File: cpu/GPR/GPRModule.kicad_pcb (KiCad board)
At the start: 2 copper layers, 139.7 x 64.3 mm, 67 parts, among them J1 Interconnect 1, J2 Interconnect 2, U1 74HCT574, U10 74LS245, U11 74LS245, U12 74LS245, U13 74LS126, U2 74HCT574, U3 74LS14, U5 74LS245, U6 74LS245, U7 74LS245, U8 74LS245, U9 74LS245

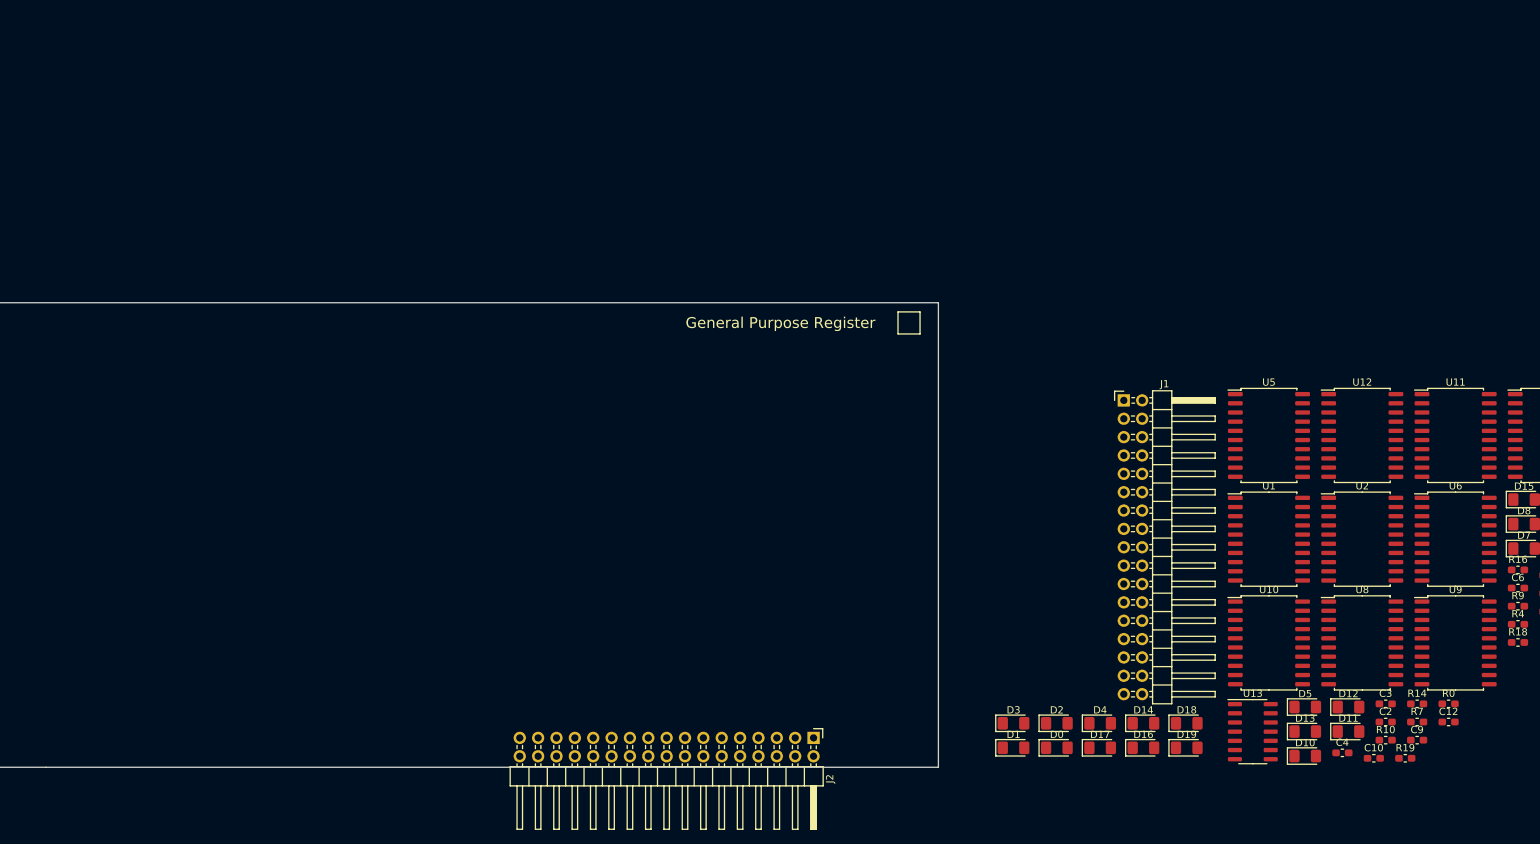
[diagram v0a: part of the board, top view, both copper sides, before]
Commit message: ALU and constant register first version
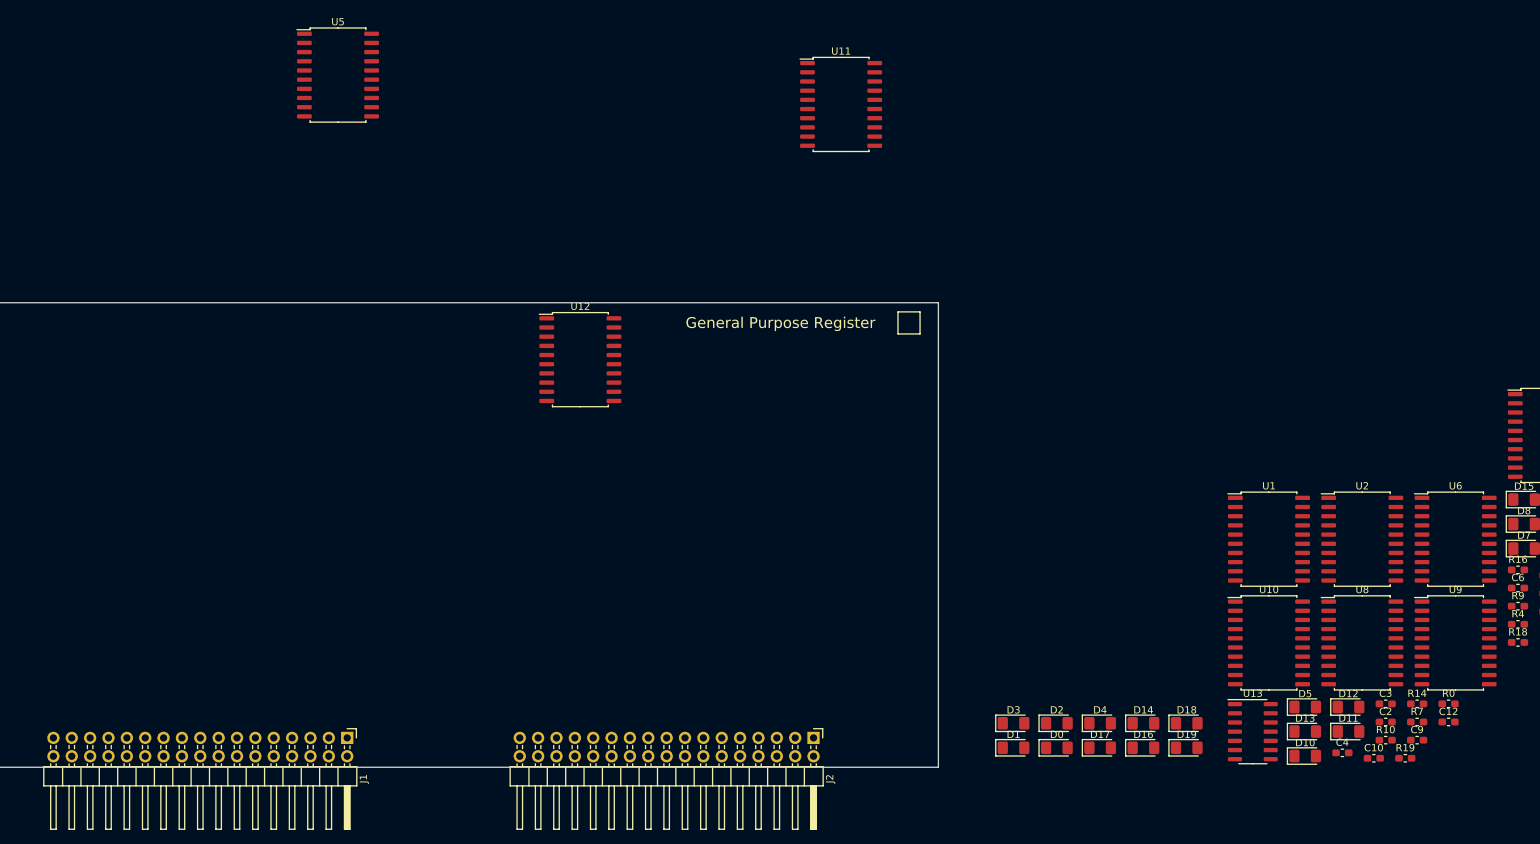
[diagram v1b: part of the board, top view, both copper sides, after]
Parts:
- moved U5 138.1 mm to (148.1, 32.3)
- moved J1 117.1 mm to (149.4, 124.0), turned to 270 degrees
- moved U12 108.7 mm to (181.6, 71.6)
- moved U11 96.6 mm to (217.7, 36.3)
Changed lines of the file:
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@@
   )
   (module Connector_PinHeader_2.54mm:PinHeader_2x17_P2.54mm_Horizontal (layer F.Cu)
-    (at 256.789001 77.263001)
+    (at 149.352 123.952 270)
     (descr "Through hole angled pin header, 2x17, 2.54mm pitch, 6mm pin length, double rows")
     (tags "Through hole angled pin header THT 2x17 2.54mm double row")
-    (fp_text reference J1 (at 5.655 -2.27) (layer F.SilkS)
-      (effects (font (size 1 1) (thickness 0.15)))
-    )
-    (fp_text value "Interconnect 1" (at 5.655 42.91) (layer F.Fab)
-      (effects (font (size 1 1) (thickness 0.15)))
-    )
-    (fp_text user %R (at 5.31 20.32 90) (layer F.Fab)
+    (fp_text reference J1 (at 5.655 -2.27 90) (layer F.SilkS)
+      (effects (font (size 1 1) (thickness 0.15)))
+    )
+    (fp_text value "Interconnect 1" (at 5.655 42.91 90) (layer F.Fab)
+      (effects (font (size 1 1) (thickness 0.15)))
+    )
+    (fp_text user %R (at 5.31 20.32) (layer F.Fab)
       (effects (font (size 1 1) (thickness 0.15)))
     )
@@
     (fp_line (start 6.58 -1.27) (end 6.58 41.91) (layer F.Fab) (width 0.1))
     (fp_line (start 4.675 -1.27) (end 6.58 -1.27) (layer F.Fab) (width 0.1))
-    (pad 34 thru_hole oval (at 2.54 40.64) (size 1.7 1.7) (drill 1) (layers *.Cu *.Mask)
+    (pad 34 thru_hole oval (at 2.54 40.64 270) (size 1.7 1.7) (drill 1) (layers *.Cu *.Mask)
       (net 2 +5V))
-    (pad 33 thru_hole oval (at 0 40.64) (size 1.7 1.7) (drill 1) (layers *.Cu *.Mask)
-      (net 1 GND))
-    (pad 32 thru_hole oval (at 2.54 38.1) (size 1.7 1.7) (drill 1) (layers *.Cu *.Mask)
+    (pad 33 thru_hole oval (at 0 40.64 270) (size 1.7 1.7) (drill 1) (layers *.Cu *.Mask)
+      (net 1 GND))
+    (pad 32 thru_hole oval (at 2.54 38.1 270) (size 1.7 1.7) (drill 1) (layers *.Cu *.Mask)
       (net 94 /d_bus_00))
-    (pad 31 thru_hole oval (at 0 38.1) (size 1.7 1.7) (drill 1) (layers *.Cu *.Mask)
+    (pad 31 thru_hole oval (at 0 38.1 270) (size 1.7 1.7) (drill 1) (layers *.Cu *.Mask)
       (net 19 /CLK))
-    (pad 30 thru_hole oval (at 2.54 35.56) (size 1.7 1.7) (drill 1) (layers *.Cu *.Mask)
+    (pad 30 thru_hole oval (at 2.54 35.56 270) (size 1.7 1.7) (drill 1) (layers *.Cu *.Mask)
       (net 95 /d_bus_01))
-    (pad 29 thru_hole oval (at 0 35.56) (size 1.7 1.7) (drill 1) (layers *.Cu *.Mask)
+    (pad 29 thru_hole oval (at 0 35.56 270) (size 1.7 1.7) (drill 1) (layers *.Cu *.Mask)
       (net 20 /~CLK))
-    (pad 28 thru_hole oval (at 2.54 33.02) (size 1.7 1.7) (drill 1) (layers *.Cu *.Mask)
+    (pad 28 thru_hole oval (at 2.54 33.02 270) (size 1.7 1.7) (drill 1) (layers *.Cu *.Mask)
       (net 96 /d_bus_02))
-    (pad 27 thru_hole oval (at 0 33.02) (size 1.7 1.7) (drill 1) (layers *.Cu *.Mask)
+    (pad 27 thru_hole oval (at 0 33.02 270) (size 1.7 1.7) (drill 1) (layers *.Cu *.Mask)
       (net 21 /HLT))
-    (pad 26 thru_hole oval (at 2.54 30.48) (size 1.7 1.7) (drill 1) (layers *.Cu *.Mask)
+    (pad 26 thru_hole oval (at 2.54 30.48 270) (size 1.7 1.7) (drill 1) (layers *.Cu *.Mask)
       (net 97 /d_bus_03))
-    (pad 25 thru_hole oval (at 0 30.48) (size 1.7 1.7) (drill 1) (layers *.Cu *.Mask)
+    (pad 25 thru_hole oval (at 0 30.48 270) (size 1.7 1.7) (drill 1) (layers *.Cu *.Mask)
       (net 114 /~DBG))
-    (pad 24 thru_hole oval (at 2.54 27.94) (size 1.7 1.7) (drill 1) (layers *.Cu *.Mask)
+    (pad 24 thru_hole oval (at 2.54 27.94 270) (size 1.7 1.7) (drill 1) (layers *.Cu *.Mask)
       (net 98 /d_bus_04))
-    (pad 23 thru_hole oval (at 0 27.94) (size 1.7 1.7) (drill 1) (layers *.Cu *.Mask)
+    (pad 23 thru_hole oval (at 0 27.94 270) (size 1.7 1.7) (drill 1) (layers *.Cu *.Mask)
       (net 22 /RST))
-    (pad 22 thru_hole oval (at 2.54 25.4) (size 1.7 1.7) (drill 1) (layers *.Cu *.Mask)
+    (pad 22 thru_hole oval (at 2.54 25.4 270) (size 1.7 1.7) (drill 1) (layers *.Cu *.Mask)
       (net 99 /d_bus_05))
-    (pad 21 thru_hole oval (at 0 25.4) (size 1.7 1.7) (drill 1) (layers *.Cu *.Mask)
+    (pad 21 thru_hole oval (at 0 25.4 270) (size 1.7 1.7) (drill 1) (layers *.Cu *.Mask)
       (net 115 "Net-(J1-Pad21)"))
-    (pad 20 thru_hole oval (at 2.54 22.86) (size 1.7 1.7) (drill 1) (layers *.Cu *.Mask)
+    (pad 20 thru_hole oval (at 2.54 22.86 270) (size 1.7 1.7) (drill 1) (layers *.Cu *.Mask)
       (net 100 /d_bus_06))
-    (pad 19 thru_hole oval (at 0 22.86) (size 1.7 1.7) (drill 1) (layers *.Cu *.Mask)
+    (pad 19 thru_hole oval (at 0 22.86 270) (size 1.7 1.7) (drill 1) (layers *.Cu *.Mask)
       (net 116 "Net-(J1-Pad19)"))
-    (pad 18 thru_hole oval (at 2.54 20.32) (size 1.7 1.7) (drill 1) (layers *.Cu *.Mask)
+    (pad 18 thru_hole oval (at 2.54 20.32 270) (size 1.7 1.7) (drill 1) (layers *.Cu *.Mask)
       (net 101 /d_bus_07))
-    (pad 17 thru_hole oval (at 0 20.32) (size 1.7 1.7) (drill 1) (layers *.Cu *.Mask)
+    (pad 17 thru_hole oval (at 0 20.32 270) (size 1.7 1.7) (drill 1) (layers *.Cu *.Mask)
       (net 117 "Net-(J1-Pad17)"))
-    (pad 16 thru_hole oval (at 2.54 17.78) (size 1.7 1.7) (drill 1) (layers *.Cu *.Mask)
+    (pad 16 thru_hole oval (at 2.54 17.78 270) (size 1.7 1.7) (drill 1) (layers *.Cu *.Mask)
       (net 102 /d_bus_08))
-    (pad 15 thru_hole oval (at 0 17.78) (size 1.7 1.7) (drill 1) (layers *.Cu *.Mask)
+    (pad 15 thru_hole oval (at 0 17.78 270) (size 1.7 1.7) (drill 1) (layers *.Cu *.Mask)
       (net 118 "Net-(J1-Pad15)"))
-    (pad 14 thru_hole oval (at 2.54 15.24) (size 1.7 1.7) (drill 1) (layers *.Cu *.Mask)
+    (pad 14 thru_hole oval (at 2.54 15.24 270) (size 1.7 1.7) (drill 1) (layers *.Cu *.Mask)
       (net 103 /d_bus_09))
-    (pad 13 thru_hole oval (at 0 15.24) (size 1.7 1.7) (drill 1) (layers *.Cu *.Mask)
+    (pad 13 thru_hole oval (at 0 15.24 270) (size 1.7 1.7) (drill 1) (layers *.Cu *.Mask)
       (net 119 "Net-(J1-Pad13)"))
-    (pad 12 thru_hole oval (at 2.54 12.7) (size 1.7 1.7) (drill 1) (layers *.Cu *.Mask)
+    (pad 12 thru_hole oval (at 2.54 12.7 270) (size 1.7 1.7) (drill 1) (layers *.Cu *.Mask)
       (net 104 /d_bus_10))
-    (pad 11 thru_hole oval (at 0 12.7) (size 1.7 1.7) (drill 1) (layers *.Cu *.Mask)
+    (pad 11 thru_hole oval (at 0 12.7 270) (size 1.7 1.7) (drill 1) (layers *.Cu *.Mask)
       (net 120 "Net-(J1-Pad11)"))
-    (pad 10 thru_hole oval (at 2.54 10.16) (size 1.7 1.7) (drill 1) (layers *.Cu *.Mask)
+    (pad 10 thru_hole oval (at 2.54 10.16 270) (size 1.7 1.7) (drill 1) (layers *.Cu *.Mask)
       (net 105 /d_bus_11))
-    (pad 9 thru_hole oval (at 0 10.16) (size 1.7 1.7) (drill 1) (layers *.Cu *.Mask)
+    (pad 9 thru_hole oval (at 0 10.16 270) (size 1.7 1.7) (drill 1) (layers *.Cu *.Mask)
       (net 121 "Net-(J1-Pad9)"))
-    (pad 8 thru_hole oval (at 2.54 7.62) (size 1.7 1.7) (drill 1) (layers *.Cu *.Mask)
+    (pad 8 thru_hole oval (at 2.54 7.62 270) (size 1.7 1.7) (drill 1) (layers *.Cu *.Mask)
       (net 106 /d_bus_12))
-    (pad 7 thru_hole oval (at 0 7.62) (size 1.7 1.7) (drill 1) (layers *.Cu *.Mask)
+    (pad 7 thru_hole oval (at 0 7.62 270) (size 1.7 1.7) (drill 1) (layers *.Cu *.Mask)
       (net 107 /y_bus_write))
-    (pad 6 thru_hole oval (at 2.54 5.08) (size 1.7 1.7) (drill 1) (layers *.Cu *.Mask)
+    (pad 6 thru_hole oval (at 2.54 5.08 270) (size 1.7 1.7) (drill 1) (layers *.Cu *.Mask)
       (net 108 /d_bus_13))
-    (pad 5 thru_hole oval (at 0 5.08) (size 1.7 1.7) (drill 1) (layers *.Cu *.Mask)
+    (pad 5 thru_hole oval (at 0 5.08 270) (size 1.7 1.7) (drill 1) (layers *.Cu *.Mask)
       (net 109 /x_bus_write))
-    (pad 4 thru_hole oval (at 2.54 2.54) (size 1.7 1.7) (drill 1) (layers *.Cu *.Mask)
+    (pad 4 thru_hole oval (at 2.54 2.54 270) (size 1.7 1.7) (drill 1) (layers *.Cu *.Mask)
       (net 110 /d_bus_14))
-    (pad 3 thru_hole oval (at 0 2.54) (size 1.7 1.7) (drill 1) (layers *.Cu *.Mask)
+    (pad 3 thru_hole oval (at 0 2.54 270) (size 1.7 1.7) (drill 1) (layers *.Cu *.Mask)
       (net 111 /d_bus_write))
-    (pad 2 thru_hole oval (at 2.54 0) (size 1.7 1.7) (drill 1) (layers *.Cu *.Mask)
+    (pad 2 thru_hole oval (at 2.54 0 270) (size 1.7 1.7) (drill 1) (layers *.Cu *.Mask)
       (net 112 /d_bus_15))
-    (pad 1 thru_hole rect (at 0 0) (size 1.7 1.7) (drill 1) (layers *.Cu *.Mask)
+    (pad 1 thru_hole rect (at 0 0 270) (size 1.7 1.7) (drill 1) (layers *.Cu *.Mask)
       (net 113 /d_bus_read))
     (model ${KISYS3DMOD}/Connector_PinHeader_2.54mm.3dshapes/PinHeader_2x17_P2.54mm_Horizontal.wrl
@@
   )
   (module Package_SO:SOIC-20W_7.5x12.8mm_P1.27mm (layer F.Cu)
-    (at 276.869001 82.113001)
+    (at 148.082 32.258)
     (descr "SOIC, 20 Pin (JEDEC MS-013AC, https://www.analog.com/media/en/package-pcb-resources/package/233848rw_20.pdf), generated with kicad-footprint-generator ipc_gullwing_generator.py")
     (tags "SOIC SO")
@@
   )
   (module Package_SO:SOIC-20W_7.5x12.8mm_P1.27mm (layer F.Cu)
-    (at 302.689001 82.113001)
+    (at 217.678 36.322)
     (descr "SOIC, 20 Pin (JEDEC MS-013AC, https://www.analog.com/media/en/package-pcb-resources/package/233848rw_20.pdf), generated with kicad-footprint-generator ipc_gullwing_generator.py")
     (tags "SOIC SO")
@@
   )
   (module Package_SO:SOIC-20W_7.5x12.8mm_P1.27mm (layer F.Cu)
-    (at 289.779001 82.113001)
+    (at 181.61 71.628)
     (descr "SOIC, 20 Pin (JEDEC MS-013AC, https://www.analog.com/media/en/package-pcb-resources/package/233848rw_20.pdf), generated with kicad-footprint-generator ipc_gullwing_generator.py")
     (tags "SOIC SO")

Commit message: Completed GPR 1.2 PCB and started lots of other things. * Started ALU * Updated Constant Reg * Completed v1.2 GPR * Added random symbols * Updated Memory * Updated plots
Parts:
- removed C12, C13: 0.1uF, Capacitor_SMD:C_0603_1608Metric_Pad1.05x0.95mm_HandSolder
- removed J2: Interconnect 2, Connector_PinHeader_2.54mm:PinHeader_2x17_P2.54mm_Horizontal
- removed R0, R1, R10, R11, R12, R13, R14, R15, R2, R3, R4, R5, R6, R7, R8, R9: 220R, Resistor_SMD:R_0603_1608Metric_Pad1.05x0.95mm_HandSolder
- removed U12: 74LS245, Package_SO:SOIC-20W_7.5x12.8mm_P1.27mm
- removed U13: 74LS126, Package_SO:SOIC-14_3.9x8.7mm_P1.27mm
- added REF**: OSHW, Symbol:OSHW-Logo2_7.3x6mm_SilkScreen, F.Cu at (178.2, 69.5)
- added RN1: 220R, Resistor_SMD:R_Array_Convex_8x0602, F.Cu at (100.2, 70.0)
- added RN2: 220R, Resistor_SMD:R_Array_Convex_8x0602, F.Cu at (128.8, 70.0)
- added U4: 74LS245, Package_SO:SOIC-20W_7.5x12.8mm_P1.27mm, F.Cu at (156.2, 92.6)
- J1: value Interconnect 1 -> Interconnect; footprint Connector_PinHeader_2.54mm:PinHeader_2x17_P2.54mm_Horizontal -> Connector_PCBEdge:BUS_PCI
- U11: value 74LS245 -> 74LS126; footprint Package_SO:SOIC-20W_7.5x12.8mm_P1.27mm -> Package_SO:SOIC-14_3.9x8.7mm_P1.27mm
- U3: value 74LS14 -> 74LS245; footprint Package_SO:SOIC-14_3.9x8.7mm_P1.27mm -> Package_SO:SOIC-20W_7.5x12.8mm_P1.27mm
- moved C8 221.7 mm to (102.6, 84.8)
- moved D15 220.3 mm to (93.9, 60.9), turned to 270 degrees
- moved U7 218.5 mm to (98.8, 109.6)
- moved C7 214.9 mm to (102.6, 101.8)
- moved D9 204.1 mm to (116.2, 60.9), turned to 270 degrees
- moved D6 197.0 mm to (129.8, 60.9), turned to 270 degrees
- moved U9 195.4 mm to (110.8, 74.2)
- moved D8 195.1 mm to (120.0, 60.9), turned to 270 degrees
- moved D12 192.1 mm to (105.0, 60.9), turned to 270 degrees
- moved U8 191.8 mm to (98.8, 92.6)
- moved D13 191.0 mm to (101.3, 60.9), turned to 270 degrees
- moved D7 189.8 mm to (126.0, 60.9), turned to 270 degrees
- moved D11 189.6 mm to (108.8, 60.9), turned to 270 degrees
- moved C9 186.8 mm to (119.1, 68.5), turned to 180 degrees
- moved C5 186.3 mm to (131.1, 101.8)
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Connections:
- C1 pad 1: +5V -> GND
- C1 pad 2: GND -> +5V
- C10 pad 1: +5V -> GND
- C10 pad 2: GND -> +5V
- C11 pad 1: +5V -> GND
- C11 pad 2: GND -> +5V
- C2 pad 1: +5V -> GND
- C2 pad 2: GND -> +5V
- C3 pad 1: +5V -> GND
- C3 pad 2: GND -> +5V
- C4 pad 1: +5V -> GND
- C4 pad 2: GND -> +5V
- C5 pad 1: +5V -> GND
- C5 pad 2: GND -> +5V
- C6 pad 1: +5V -> GND
- C6 pad 2: GND -> +5V
- C7 pad 1: +5V -> GND
- C7 pad 2: GND -> +5V
- C8 pad 1: +5V -> GND
- C8 pad 2: GND -> +5V
- C9 pad 1: +5V -> GND
- C9 pad 2: GND -> +5V
- D0 pad 1: Net-(D0-Pad1) -> GND
- D0 pad 2: /display_00 -> Net-(D0-Pad2)
- D1 pad 1: Net-(D1-Pad1) -> GND
- D1 pad 2: /display_01 -> Net-(D1-Pad2)
- D10 pad 1: Net-(D10-Pad1) -> GND
- D10 pad 2: /display_10 -> Net-(D10-Pad2)
- D11 pad 1: Net-(D11-Pad1) -> GND
- D11 pad 2: /display_11 -> Net-(D11-Pad2)
- D12 pad 1: Net-(D12-Pad1) -> GND
- D12 pad 2: /display_12 -> Net-(D12-Pad2)
- D13 pad 1: Net-(D13-Pad1) -> GND
- D13 pad 2: /display_13 -> Net-(D13-Pad2)
- D14 pad 1: Net-(D14-Pad1) -> GND
- D14 pad 2: /display_14 -> Net-(D14-Pad2)
- D15 pad 1: Net-(D15-Pad1) -> GND
- D15 pad 2: /display_15 -> Net-(D15-Pad2)
- D16 pad 2: Net-(D16-Pad2) -> +5V
- D17 pad 2: Net-(D17-Pad2) -> +5V
- D18 pad 2: Net-(D18-Pad2) -> +5V
- D19 pad 1: Net-(D19-Pad1) -> GND
- D2 pad 1: Net-(D2-Pad1) -> GND
- D2 pad 2: /display_02 -> Net-(D2-Pad2)
- D3 pad 1: Net-(D3-Pad1) -> GND
- D3 pad 2: /display_03 -> Net-(D3-Pad2)
- D4 pad 1: Net-(D4-Pad1) -> GND
- D4 pad 2: /display_04 -> Net-(D4-Pad2)
- D5 pad 1: Net-(D5-Pad1) -> GND
- D5 pad 2: /display_05 -> Net-(D5-Pad2)
- D6 pad 1: Net-(D6-Pad1) -> GND
- D6 pad 2: /display_06 -> Net-(D6-Pad2)
- D7 pad 1: Net-(D7-Pad1) -> GND
- D7 pad 2: /display_07 -> Net-(D7-Pad2)
- D8 pad 1: Net-(D8-Pad1) -> GND
- D8 pad 2: /display_08 -> Net-(D8-Pad2)
- D9 pad 1: Net-(D9-Pad1) -> GND
- D9 pad 2: /display_09 -> Net-(D9-Pad2)
- R16 pad 1: Net-(D16-Pad1) -> Net-(R16-Pad1)
- R16 pad 2: GND -> Net-(D16-Pad1)
- R17 pad 1: Net-(D17-Pad1) -> Net-(R17-Pad1)
- R17 pad 2: GND -> Net-(D17-Pad1)
- R18 pad 1: Net-(D18-Pad1) -> Net-(R18-Pad1)
- R18 pad 2: GND -> Net-(D18-Pad1)
- R19 pad 1: Net-(D19-Pad1) -> Net-(R19-Pad1)
- R19 pad 2: GND -> Net-(D19-Pad2)
- U10 pad 12: /reg_14 -> /reg_06
- U10 pad 13: /reg_13 -> /reg_05
- U10 pad 14: /reg_12 -> /reg_04
- U10 pad 15: /reg_11 -> /reg_03
- U10 pad 16: /reg_10 -> /reg_02
- U10 pad 17: /reg_09 -> /reg_01
- U10 pad 18: /reg_08 -> /reg_00
- U10 pad 19: /~y_bus_write -> /~DBG
- U10 pad 2: /y_bus_08 -> /display_00
- U10 pad 3: /y_bus_09 -> /display_01
- U10 pad 4: /y_bus_10 -> /display_02
- U10 pad 5: /y_bus_11 -> /display_03
- U10 pad 6: /y_bus_12 -> /display_04
- U10 pad 7: /y_bus_13 -> /display_05
- U10 pad 8: /y_bus_14 -> /display_06
- U10 pad 9: /y_bus_15 -> /display_07
- U11 pad 1: GND -> /~DBG
- U11 pad 10: GND -> /~DBG
- U11 pad 11: /reg_07 -> Net-(R19-Pad1)
- U11 pad 12: /reg_06 -> /d_bus_read
- U11 pad 13: /reg_05 -> /~DBG
- U11 pad 14: /reg_04 -> +5V
- U11 pad 2: /display_00 -> /~x_bus_write
- U11 pad 3: /display_01 -> Net-(R16-Pad1)
- U11 pad 4: /display_02 -> /~DBG
- U11 pad 5: /display_03 -> /~y_bus_write
- U11 pad 6: /display_04 -> Net-(R17-Pad1)
- U11 pad 7: /display_05 -> GND
- U11 pad 8: /display_06 -> Net-(R18-Pad1)
- U11 pad 9: /display_07 -> /~d_bus_write
- U2 pad 12: /reg_07 -> /reg_15
- U3 pad 1: /d_bus_write -> GND
- U3 pad 10: Net-(U3-Pad10) -> GND
- U3 pad 11: Net-(U3-Pad11) -> /reg_15
- U3 pad 12: Net-(U3-Pad12) -> /reg_14
- U3 pad 13: Net-(U3-Pad13) -> /reg_13
- U3 pad 14: +5V -> /reg_12
- U3 pad 2: /~d_bus_write -> /d_bus_08
- U3 pad 3: /x_bus_write -> /d_bus_09
- U3 pad 4: /~x_bus_write -> /d_bus_10
- U3 pad 5: /y_bus_write -> /d_bus_11
- U3 pad 6: /~y_bus_write -> /d_bus_12
- U3 pad 7: GND -> /d_bus_13
- U3 pad 8: Net-(U3-Pad8) -> /d_bus_14
- U3 pad 9: Net-(U3-Pad9) -> /d_bus_15
- U5 pad 11: /reg_07 -> /reg_15
- U5 pad 12: /reg_06 -> /reg_14
- U5 pad 13: /reg_05 -> /reg_13
- U5 pad 14: /reg_04 -> /reg_12
- U5 pad 15: /reg_03 -> /reg_11
- U5 pad 16: /reg_02 -> /reg_10
- U5 pad 17: /reg_01 -> /reg_09
- U5 pad 18: /reg_00 -> /reg_08
- U5 pad 19: /~d_bus_write -> /~x_bus_write
- U5 pad 2: /d_bus_00 -> /x_bus_08
- U5 pad 3: /d_bus_01 -> /x_bus_09
- U5 pad 4: /d_bus_02 -> /x_bus_10
- U5 pad 5: /d_bus_03 -> /x_bus_11
- U5 pad 6: /d_bus_04 -> /x_bus_12
- U5 pad 7: /d_bus_05 -> /x_bus_13
- U5 pad 8: /d_bus_06 -> /x_bus_14
- U5 pad 9: /d_bus_07 -> /x_bus_15
- U6 pad 12: /reg_14 -> /reg_06
- U6 pad 13: /reg_13 -> /reg_05
- U6 pad 14: /reg_12 -> /reg_04
- U6 pad 15: /reg_11 -> /reg_03
- U6 pad 16: /reg_10 -> /reg_02
- U6 pad 17: /reg_09 -> /reg_01
- U6 pad 18: /reg_08 -> /reg_00
- U6 pad 19: /~d_bus_write -> /~x_bus_write
- U6 pad 2: /d_bus_08 -> /x_bus_00
- U6 pad 3: /d_bus_09 -> /x_bus_01
- U6 pad 4: /d_bus_10 -> /x_bus_02
- U6 pad 5: /d_bus_11 -> /x_bus_03
- U6 pad 6: /d_bus_12 -> /x_bus_04
- U6 pad 7: /d_bus_13 -> /x_bus_05
- U6 pad 8: /d_bus_14 -> /x_bus_06
- U6 pad 9: /d_bus_15 -> /x_bus_07
- U7 pad 11: /reg_07 -> /reg_15
- U7 pad 12: /reg_06 -> /reg_14
- U7 pad 13: /reg_05 -> /reg_13
- U7 pad 14: /reg_04 -> /reg_12
- U7 pad 15: /reg_03 -> /reg_11
- U7 pad 16: /reg_02 -> /reg_10
- U7 pad 17: /reg_01 -> /reg_09
- U7 pad 18: /reg_00 -> /reg_08
- U7 pad 19: /~x_bus_write -> /~y_bus_write
- U7 pad 2: /x_bus_00 -> /y_bus_08
- U7 pad 3: /x_bus_01 -> /y_bus_09
- U7 pad 4: /x_bus_02 -> /y_bus_10
- U7 pad 5: /x_bus_03 -> /y_bus_11
- U7 pad 6: /x_bus_04 -> /y_bus_12
- U7 pad 7: /x_bus_05 -> /y_bus_13
- U7 pad 8: /x_bus_06 -> /y_bus_14
- U7 pad 9: /x_bus_07 -> /y_bus_15
- U8 pad 12: /reg_14 -> /reg_06
- U8 pad 13: /reg_13 -> /reg_05
- U8 pad 14: /reg_12 -> /reg_04
- U8 pad 15: /reg_11 -> /reg_03
- U8 pad 16: /reg_10 -> /reg_02
- U8 pad 17: /reg_09 -> /reg_01
- U8 pad 18: /reg_08 -> /reg_00
- U8 pad 19: /~x_bus_write -> /~y_bus_write
- U8 pad 2: /x_bus_08 -> /y_bus_00
- U8 pad 3: /x_bus_09 -> /y_bus_01
- U8 pad 4: /x_bus_10 -> /y_bus_02
- U8 pad 5: /x_bus_11 -> /y_bus_03
- U8 pad 6: /x_bus_12 -> /y_bus_04
- U8 pad 7: /x_bus_13 -> /y_bus_05
- U8 pad 8: /x_bus_14 -> /y_bus_06
- U8 pad 9: /x_bus_15 -> /y_bus_07
- U9 pad 11: /reg_07 -> /reg_15
- U9 pad 12: /reg_06 -> /reg_14
- U9 pad 13: /reg_05 -> /reg_13
- U9 pad 14: /reg_04 -> /reg_12
- U9 pad 15: /reg_03 -> /reg_11
- U9 pad 16: /reg_02 -> /reg_10
- U9 pad 17: /reg_01 -> /reg_09
- U9 pad 18: /reg_00 -> /reg_08
- U9 pad 19: /~y_bus_write -> /~DBG
- U9 pad 2: /y_bus_00 -> /display_08
- U9 pad 3: /y_bus_01 -> /display_09
- U9 pad 4: /y_bus_02 -> /display_10
- U9 pad 5: /y_bus_03 -> /display_11
- U9 pad 6: /y_bus_04 -> /display_12
- U9 pad 7: /y_bus_05 -> /display_13
- U9 pad 8: /y_bus_06 -> /display_14
- U9 pad 9: /y_bus_07 -> /display_15
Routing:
- net +5V: track 0.00 -> 357.6 mm, vias 0 -> 1
- net /~y_bus_write: track 0.00 -> 166.9 mm, vias 0 -> 3
- net /~DBG: track 0.00 -> 154.4 mm, vias 0 -> 4
- net /reg_14: track 0.00 -> 132.4 mm, vias 0 -> 4
- net /reg_15: track 0.00 -> 132.4 mm, vias 0 -> 4
- net /reg_13: track 0.00 -> 132.0 mm, vias 0 -> 4
- net /reg_11: track 0.00 -> 131.9 mm, vias 0 -> 4
- net /reg_09: track 0.00 -> 131.9 mm, vias 0 -> 4
- net /reg_12: track 0.00 -> 131.9 mm, vias 0 -> 4
- net /reg_10: track 0.00 -> 131.9 mm, vias 0 -> 4
- net /reg_08: track 0.00 -> 131.8 mm, vias 0 -> 4
- net /d_bus_read: track 0.00 -> 118.9 mm, vias 0 -> 3
- net /~x_bus_write: track 0.00 -> 117.1 mm, vias 0 -> 3
- net /reg_07: track 0.00 -> 115.3 mm, vias 0 -> 4
- net /reg_06: track 0.00 -> 115.2 mm, vias 0 -> 4
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- added copper zone on B.Cu, net GND
- added copper zone on F.Cu, net GND
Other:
- board size 139.7 x 64.3 mm -> 100 x 80 mm
- net class Power added: clearance 0.2, trace_width 0.5, via_dia 1.6, via_drill 0.8
- rule trace_min: 0.2 -> 0.127
- rule via_min_drill: 0.3 -> 0.2
- rule via_min_size: 0.4 -> 0.45
- board text added: "07 06 05 04 03 02 01 00"
- board text added: "15 14 13 12 11 10 09 08"
- board text added: "Beveled Fingers (chamfers)"
- board text added: "CPU u16"
- board text added: "d_bus d_bus y_bus x_bus"
- board text added: "read write write write"
- board text removed: "DaisyX"
